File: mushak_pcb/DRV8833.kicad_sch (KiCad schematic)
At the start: 7 parts, among them M1 motor, M2 motor, U3 DRV8833PW

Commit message: changed footprint of passive components
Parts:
- C27, C28: footprint Capacitor_SMD:C_0402_1005Metric -> Capacitor_SMD:C_0603_1608Metric
- R25: footprint Resistor_SMD:R_0201_0603Metric -> Resistor_SMD:R_0402_1005Metric
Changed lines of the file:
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@@
       (effects (font (size 1.27 1.27)) (justify right))
     )
-    (property "Footprint" "Resistor_SMD:R_0201_0603Metric" (id 2) (at 133.858 83.82 90)
+    (property "Footprint" "Resistor_SMD:R_0402_1005Metric" (id 2) (at 133.858 83.82 90)
       (effects (font (size 1.27 1.27)) hide)
     )
@@
     (property "Reference" "C27" (id 0) (at 143.764 68.58 90))
     (property "Value" "2.2uF" (id 1) (at 143.764 71.12 90))
-    (property "Footprint" "Capacitor_SMD:C_0402_1005Metric" (id 2) (at 147.574 74.7268 0)
+    (property "Footprint" "Capacitor_SMD:C_0603_1608Metric" (id 2) (at 147.574 74.7268 0)
       (effects (font (size 1.27 1.27)) hide)
     )
@@
     (property "Reference" "C28" (id 0) (at 163.322 68.58 90))
     (property "Value" "10uF" (id 1) (at 163.322 71.12 90))
-    (property "Footprint" "Capacitor_SMD:C_0402_1005Metric" (id 2) (at 167.132 74.7268 0)
+    (property "Footprint" "Capacitor_SMD:C_0603_1608Metric" (id 2) (at 167.132 74.7268 0)
       (effects (font (size 1.27 1.27)) hide)
     )

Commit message: Started Poer trace routing
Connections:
- net at U3.5 (BOUT2): now also M2.1 (VMOT+); no longer M2.2 (VMOT-)
- net at U3.7 (BOUT1): now also M2.2 (VMOT-); no longer M2.1 (VMOT+)
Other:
- moved on the sheet: M2
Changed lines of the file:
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@@
     (pin "9")
   )
-  (symbol (lib_id "New_Library:motor") (at 212.598 120.904 0) (unit 1)
+  (symbol (lib_id "New_Library:motor") (at 212.598 120.904 180) (unit 1)
     (in_bom yes) (on_board yes) (fields_autoplaced)
     (property "Reference" "M2" (id 0) (at 212.598 107.95 0))

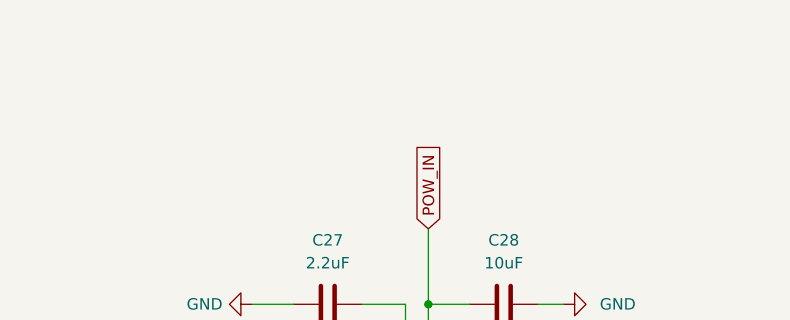
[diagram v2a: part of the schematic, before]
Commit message: changed oscilattor placement
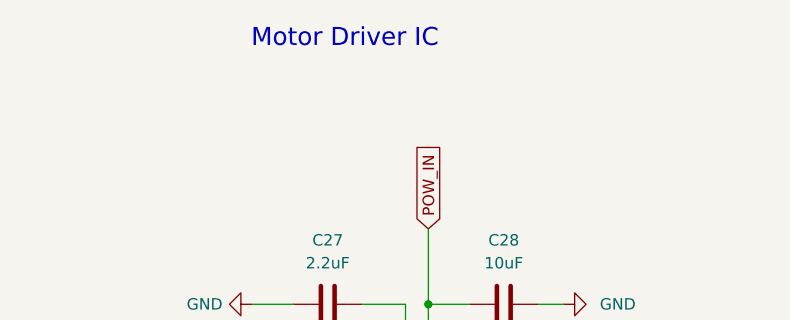
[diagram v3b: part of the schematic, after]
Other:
- note added: "Motor Driver IC"
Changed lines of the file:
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@@
     (stroke (width 0) (type default) (color 0 0 0 0))
+  )
+  (text "Motor Driver IC" (at 135.255 47.371 0)
+    (effects (font (size 2 2)) (justify left bottom))
   )
   (global_label "POW_IN" (shape input) (at 120.904 90.17 180) (fields_autoplaced)
